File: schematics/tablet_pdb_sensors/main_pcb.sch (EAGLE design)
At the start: 10 parts

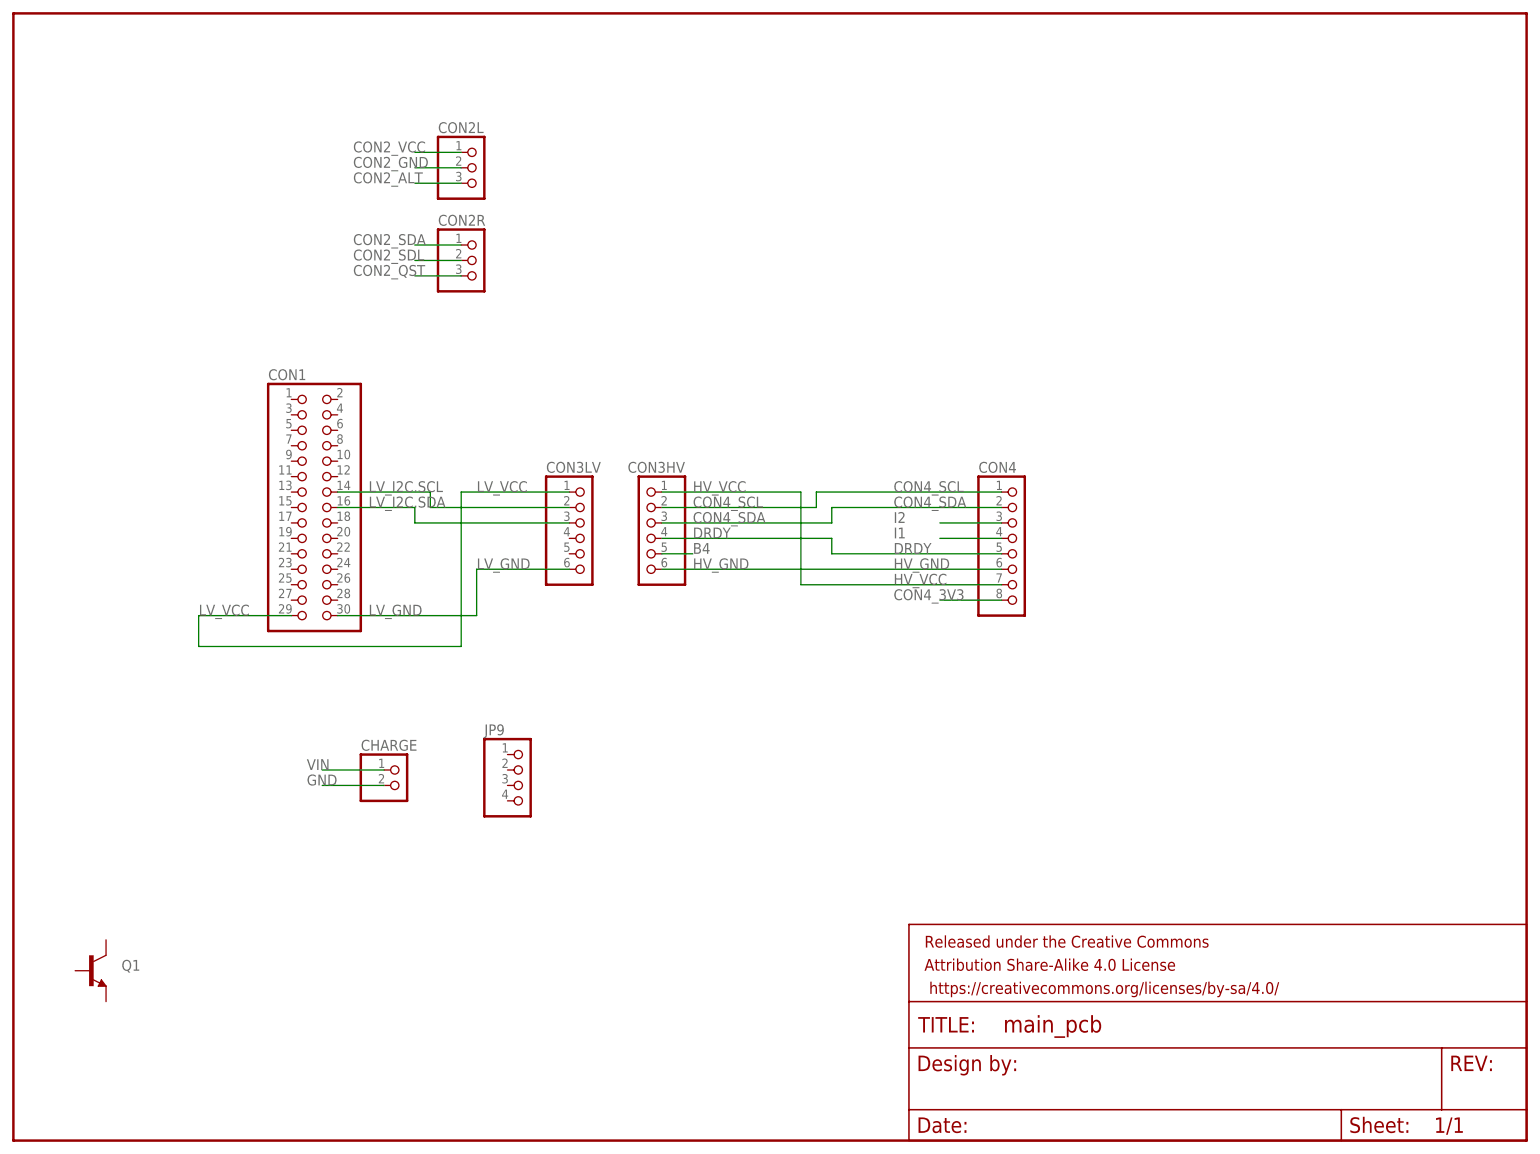
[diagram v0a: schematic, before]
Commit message: Wired up fuel cell and charger
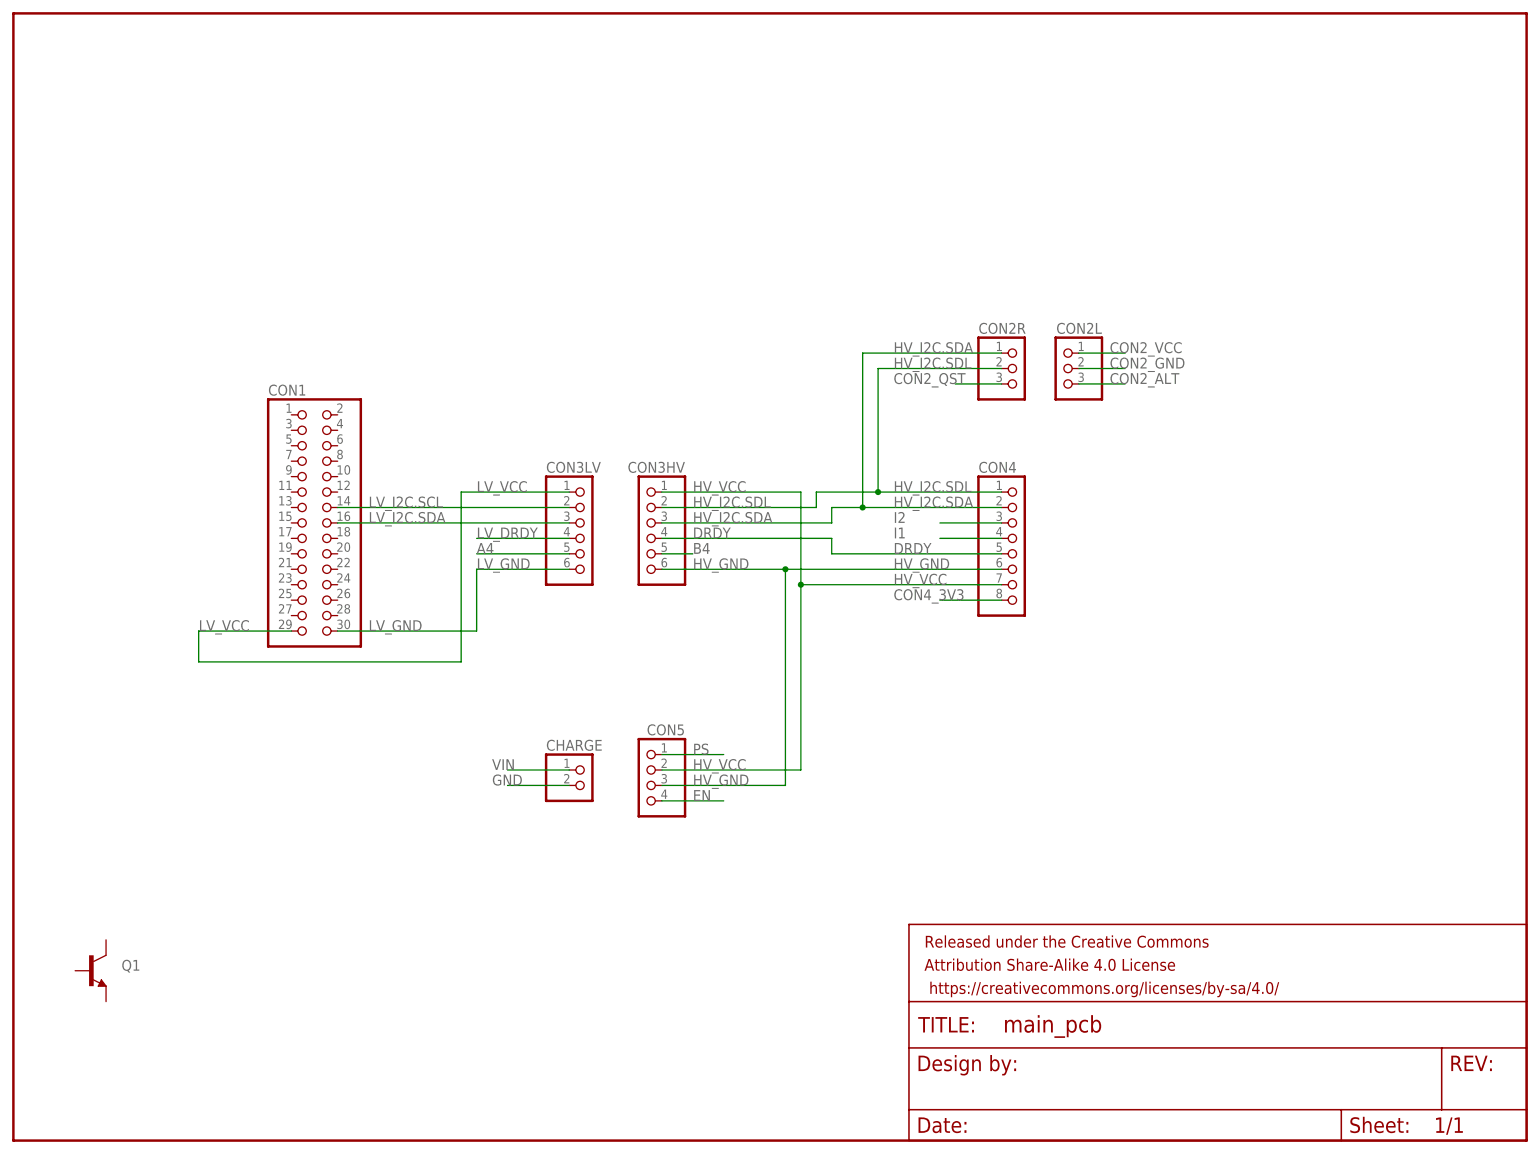
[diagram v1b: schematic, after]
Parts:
- removed JP9: (no value), pinhead:PINHD-1X4
- added CON5: (no value), pinhead:PINHD-1X4
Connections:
- removed net CON2_SDA: CON2R.1
- removed net CON2_SDL: CON2R.2
- removed net CON4_SCL: CON3HV.2, CON4.1
- removed net CON4_SDA: CON3HV.3, CON4.2
- new net A4: CON3LV.5
- new net EN: CON5.4
- new net HV_I2C.SDA: CON2R.1, CON3HV.3, CON4.2
- new net HV_I2C.SDL: CON2R.2, CON3HV.2, CON4.1
- new net LV_DRDY: CON3LV.4
- new net PS: CON5.1
- net HV_GND: now also CON5.3
- net HV_VCC: now also CON5.2
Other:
- moved on the sheet: CHARGE, CON1, CON2L, CON2R

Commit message: Completed schematic
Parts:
- removed CHARGE: (no value), pinhead:PINHD-1X2
- removed CON5: (no value), pinhead:PINHD-1X4
- removed Q1: (no value), SparkFun-DiscreteSemi:TRANSISTOR_NPN2N3904
- added CON5L, CON6, CON7LED, CON7SWITCH, CON8: (no value), pinhead:PINHD-1X2
- added CON5R: (no value), pinhead:PINHD-1X4
- added H1, H2, H3, H4: MOUNT-HOLE2.8, holes:MOUNT-HOLE2.8
- added LOGO1: OSHW-LOGOL, SparkFun-Aesthetics:OSHW-LOGOL
- added R.LED, R.PULLUP: (no value), resistor:R-US_0204/2V
- CON1: device pinhead-2:PINHD-2X15_2.00 -> pinhead:PINHD-2X20
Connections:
- new net N$1: CON7LED.1, R.LED.2
- new net SIG.LED1: CON1.16, R.LED.1
- new net SIG.LED2: CON1.18, CON7LED.2
- new net SIG.SWITCH: CON1.15, CON7SWITCH.1, R.PULLUP.1
- net EN: now also CON5R.4; no longer CON5.4
- net GND: now also CON5L.2, CON6.2; no longer CHARGE.2
- net HV_GND: now also CON5R.3, CON8.2; no longer CON5.3
- net HV_VCC: now also CON5R.2, CON8.1; no longer CON5.2
- net LV_GND: now also CON1.25, CON7SWITCH.2; no longer CON1.30
- net LV_I2C.SCL: now also CON1.5; no longer CON1.14
- net LV_I2C.SDA: now also CON1.3; no longer CON1.16
- net LV_VCC: now also CON1.1, R.PULLUP.2; no longer CON1.29
- net PS: now also CON5R.1; no longer CON5.1
- net VIN: now also CON5L.1, CON6.1; no longer CHARGE.1
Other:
- moved on the sheet: CON2L, CON2R, CON3HV, CON3LV, CON4
